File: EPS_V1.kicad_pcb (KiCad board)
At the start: 2 copper layers, 82.5 x 82.5 mm, 195 parts, among them J1 Conn_01x19, J2 Conn_01x25, J3 Conn_01x9, J4 Conn_01x02, SW1 SWITCH, SW2 SWITCH, SW3 SWITCH, U1 MP2672AGD-0000-Z, U10 MP2672AGD-0000-Z, U11 MAX17205G+, U12 MP2672AGD-0000-Z, U13 MAX17205G+, U2 TPS62132RGTR, U3 TPS62133RGTR, U4 MP28167GQ-Z, U5 MAX17205G+, U6 TPS61088RHLR, U7 TPS2121RUXR, U8 MP2672AGD-0000-Z, U9 MAX17205G+

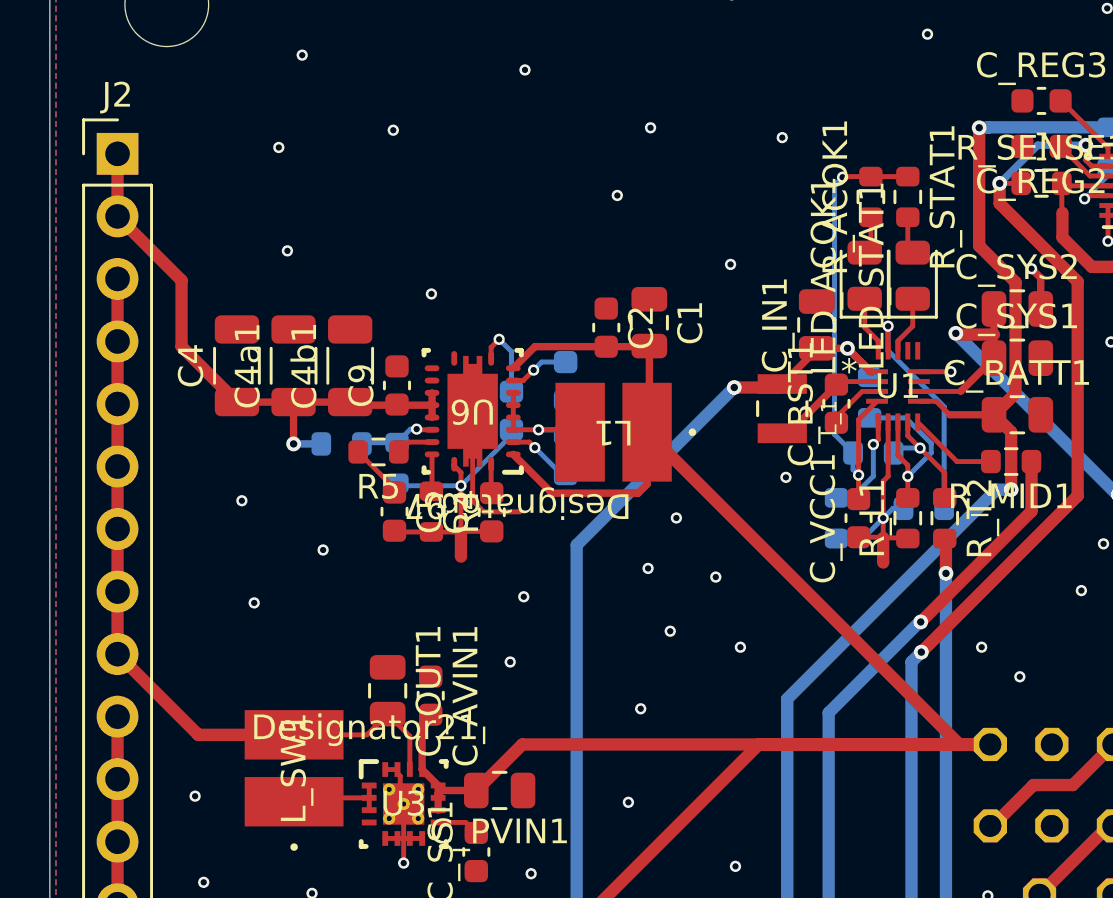
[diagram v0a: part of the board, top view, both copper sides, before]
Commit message: Expose unregulated battery voltage for burn wire
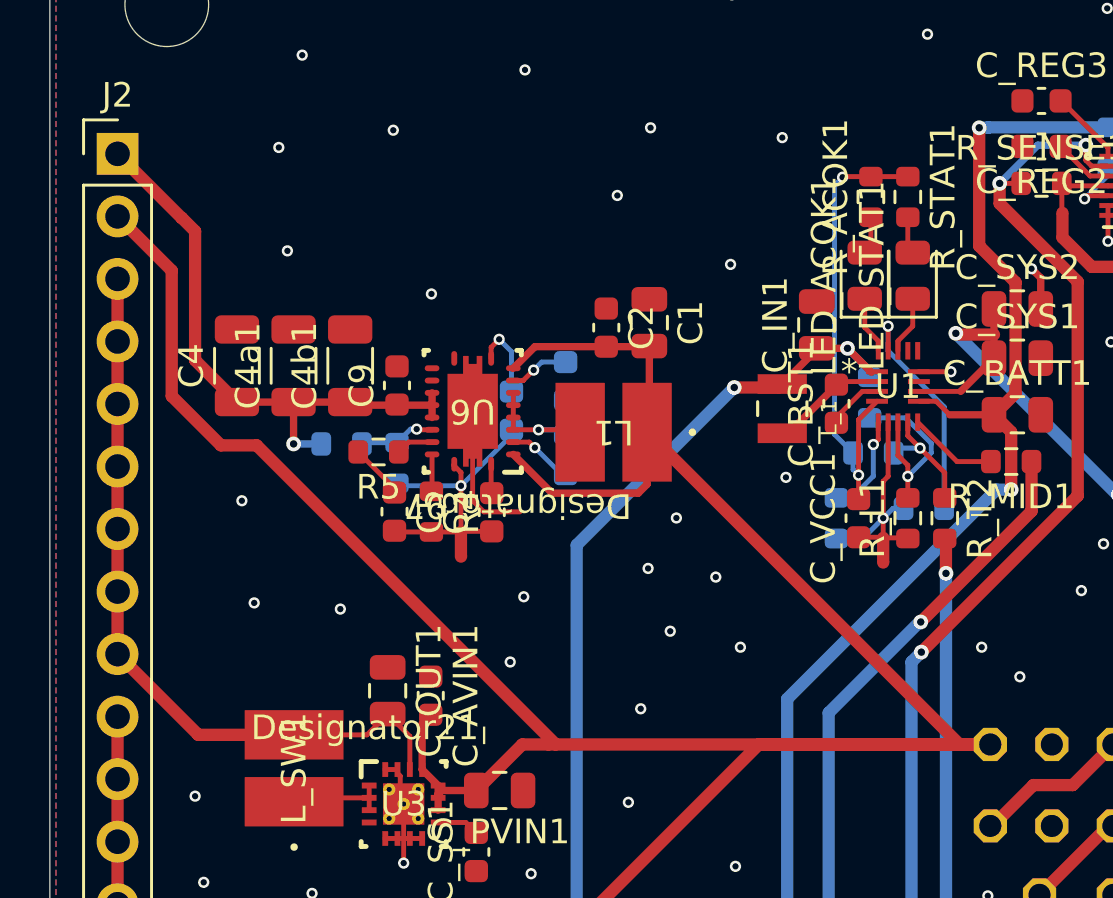
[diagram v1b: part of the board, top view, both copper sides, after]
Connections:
- J2 pad 2: +12V -> CHG_OUT
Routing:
- net CHG_OUT: track 146.5 -> 176.2 mm

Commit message: Fix NC pins, add 2 test points & silkscreen labels
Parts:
- added TP1: TestPoint, TestPoint:TestPoint_Pad_D1.5mm, F.Cu at (114.3, 121.7)
- added TP2: TestPoint, TestPoint:TestPoint_Pad_D1.5mm, F.Cu at (110.5, 109.2)
- moved J1 1.50 mm to (76.5, 136.8)
- moved J2 1.20 mm to (62.7, 69.6)
- moved D_SCL2 1.10 mm to (133.9, 95.6)
- moved D_SDA1 1.10 mm to (133.9, 80.4)
- moved R_SCL2 1.10 mm to (133.9, 95.6)
- moved R_SDA1 1.10 mm to (133.9, 80.4)
- moved D_ALRT1 1.10 mm to (133.9, 90.5)
- moved D_SCL1 1.10 mm to (133.9, 82.9)
- moved D_SCL3 1.10 mm to (133.9, 88.0)
- moved D_SCL4 1.10 mm to (133.9, 100.7)
- moved D_SDA2 1.10 mm to (133.9, 93.1)
- moved D_SDA3 1.10 mm to (133.9, 85.5)
- moved D_SDA4 1.10 mm to (133.9, 98.2)
- moved J3 1.10 mm to (137.2, 80.4)
- moved R_ALRT1 1.10 mm to (133.9, 90.5)
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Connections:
- U1 pad 14: unconnected-(U1-SCL-Pad14) -> GND
- U1 pad 15: unconnected-(U1-SDA-Pad15) -> GND
- U10 pad 14: unconnected-(U10-SCL-Pad14) -> GND
- U10 pad 15: unconnected-(U10-SDA-Pad15) -> GND
- U11 pad 10: unconnected-(U11-AIN2-Pad10) -> GND
- U11 pad 9: unconnected-(U11-AIN1-Pad9) -> GND
- U12 pad 14: unconnected-(U12-SCL-Pad14) -> GND
- U12 pad 15: unconnected-(U12-SDA-Pad15) -> GND
- U13 pad 10: unconnected-(U13-AIN2-Pad10) -> GND
- U13 pad 9: unconnected-(U13-AIN1-Pad9) -> GND
- U2 pad 4: unconnected-(U2-PG-Pad4) -> GND
- U2 pad V: (no net) -> GND
- U3 pad 18: (no net) -> GND
- U3 pad 19: (no net) -> GND
- U3 pad 20: (no net) -> GND
- U3 pad 21: (no net) -> GND
- U3 pad 22: (no net) -> GND
- U3 pad 4: unconnected-(U3-PG-Pad4) -> GND
- U4 pad 4: unconnected-(U4-NC-Pad4) -> GND
- U4 pad 8: unconnected-(U4-NC-Pad8) -> GND
- U5 pad 10: unconnected-(U5-AIN2-Pad10) -> GND
- U5 pad 9: unconnected-(U5-AIN1-Pad9) -> GND
- U6 pad 11: unconnected-(U6-NC-Pad11) -> GND
- U6 pad 12: unconnected-(U6-NC-Pad12) -> GND
- U8 pad 14: unconnected-(U8-SCL-Pad14) -> GND
- U8 pad 15: unconnected-(U8-SDA-Pad15) -> GND
- U9 pad 10: unconnected-(U9-AIN2-Pad10) -> GND
- U9 pad 9: unconnected-(U9-AIN1-Pad9) -> GND
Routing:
- net GND: track 47.5 -> 67.5 mm, vias 172 -> 182
- net ALRT: track 151.3 -> 148.7 mm
- net CHG_OUT: track 176.2 -> 174.6 mm
- net BATT2M: track 29.0 -> 27.5 mm
- net BATT3-: track 79.2 -> 77.7 mm
- net SOLAR: track 26.2 -> 24.7 mm
- net NTC3: track 57.9 -> 56.4 mm
- net NTC1: track 53.5 -> 52.0 mm
- net BATT4M: track 29.7 -> 28.2 mm
- net BATT4-: track 28.5 -> 27.0 mm
- net BATT4+: track 42.7 -> 41.2 mm
- net BATT3M: track 66.7 -> 65.2 mm
- net BATT3+: track 92.6 -> 91.1 mm
- net BATT2+: track 38.5 -> 37.0 mm
- net BATT1M: track 60.2 -> 58.7 mm
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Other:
- board text added: "1+"
- board text added: "1-"
- board text added: "12V"
- board text added: "1M"
- board text added: "2+"
- board text added: "2-"
- board text added: "2M"
- board text added: "3+"
- board text added: "3-"
- board text added: "3M"
- board text added: "3V3"
- board text added: "4+"
- board text added: "4-"
- board text added: "4M"
- board text added: "5V"
- board text added: "BATT"
- board text added: "G"
- board text added: "GND"
- board text added: "S"
- board text added: "T1"
- board text added: "T2"
- board text added: "T3"
- board text added: "T4"

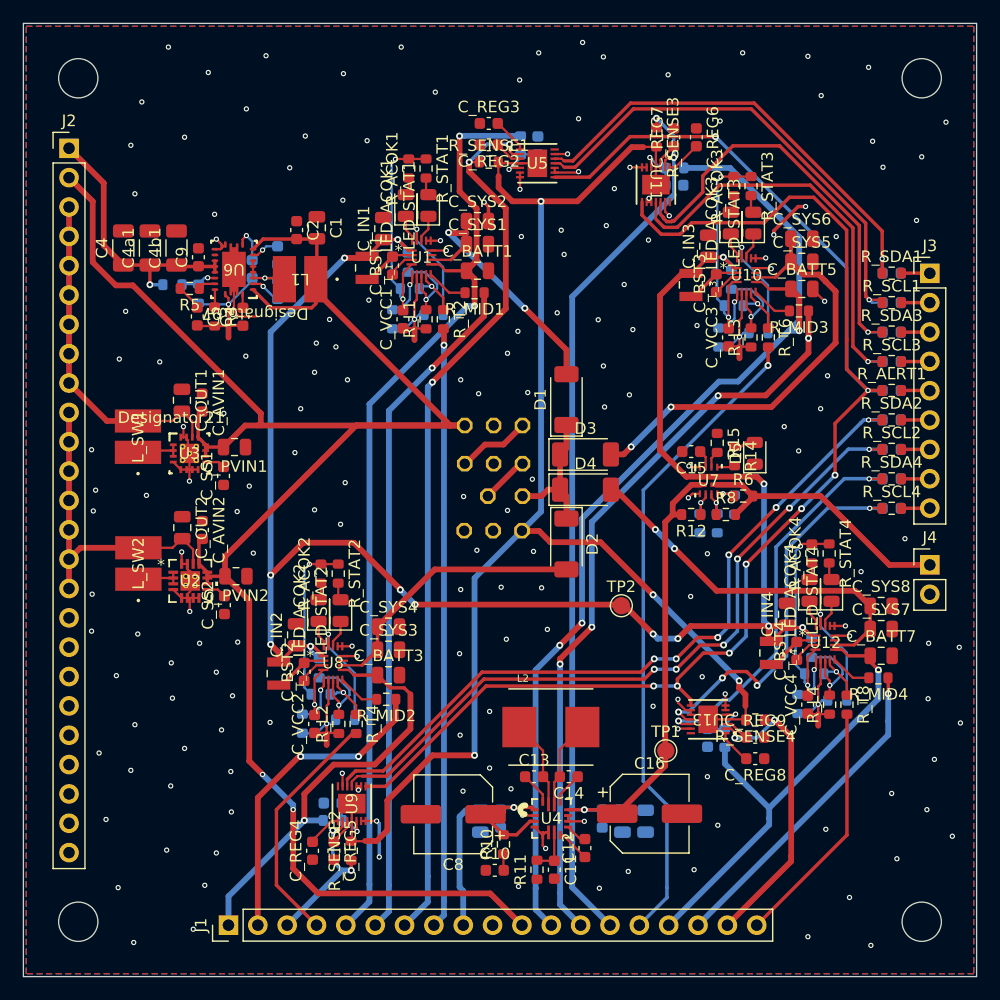
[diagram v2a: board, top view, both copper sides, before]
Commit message: Fix silkscreen; Fix component value style
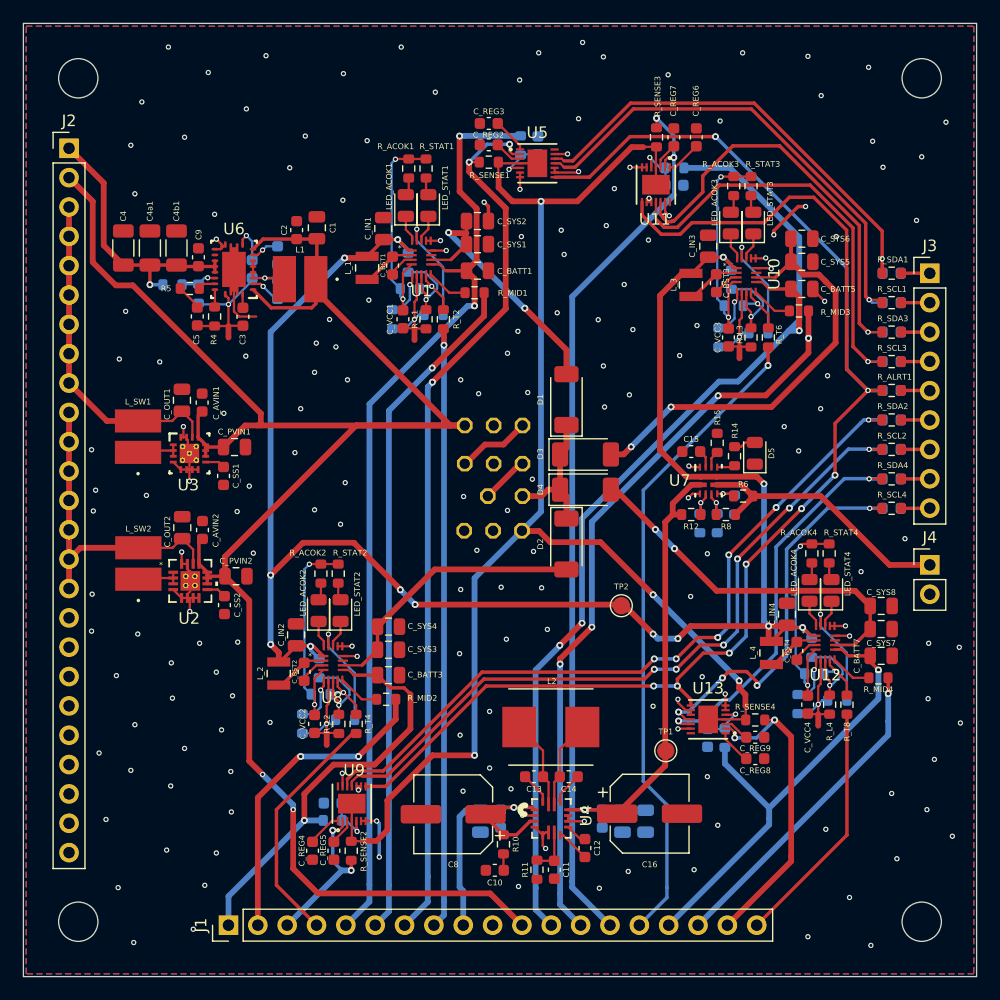
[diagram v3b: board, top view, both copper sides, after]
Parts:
- C13, C14, C1A1, C2, C2A1, C6, C_AVIN1, C_AVIN2, C_BATT2, C_BATT4, C_BATT6, C_BATT8, C_BST1, C_BST2, C_BST3, C_BST4: value 0.1u -> 100n
- C_REG2, C_REG3, C_REG4, C_REG5, C_REG6, C_REG7, C_REG8, C_REG9: value 0.47u -> 470n
- R_BATT1, R_BATT2, R_BATT3, R_BATT4, R_MID1, R_MID2, R_MID3, R_MID4: value 50 -> 50R
- R_SCL1, R_SCL2, R_SCL3, R_SCL4, R_SDA1, R_SDA2, R_SDA3, R_SDA4: value 150 -> 150R
- R_SENSE1, R_SENSE2, R_SENSE3, R_SENSE4: value 0.01 -> 10m
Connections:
- U2 pad V: GND -> (no net)
- U3 pad 18: GND -> (no net)
- U3 pad 19: GND -> (no net)
- U3 pad 20: GND -> (no net)
- U3 pad 21: GND -> (no net)
- U3 pad 22: GND -> (no net)

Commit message: fix silkscreen again...
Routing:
- net BATT3M: vias 4 -> 3
